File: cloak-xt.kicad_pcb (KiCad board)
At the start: 2 copper layers, 289.7 x 98 mm, 187 parts, among them J1 JST, Q1 Q_PMOS_GSD, Q2 Q_PMOS_GSD, U1 STM32F072CBT6, U3 XC6206PxxxMR-Regulator_Linear

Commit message: Fixed and ignore silkscreen clipping
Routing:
- net COL2: track 324.5 -> 321.8 mm
- net ROW2: track 375.8 -> 373.7 mm
- net COL1: track 329.9 -> 328.1 mm
- net COL0: track 384.0 -> 382.2 mm
- net Net-(D29-A): track 29.4 -> 28.4 mm
- net COL4: track 271.9 -> 271.0 mm
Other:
- board text added: "switch center"

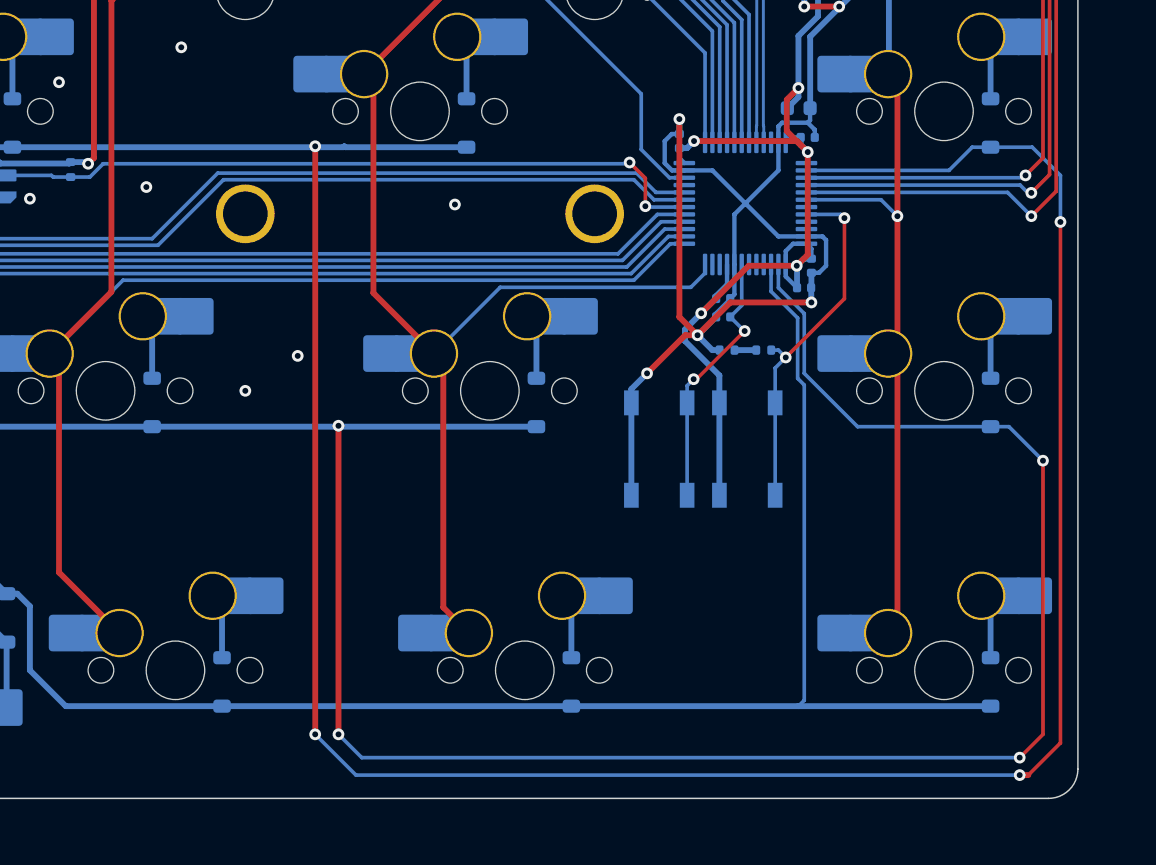
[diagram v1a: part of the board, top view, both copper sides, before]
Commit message: Fix PF/PC pins and change LED pin to B8
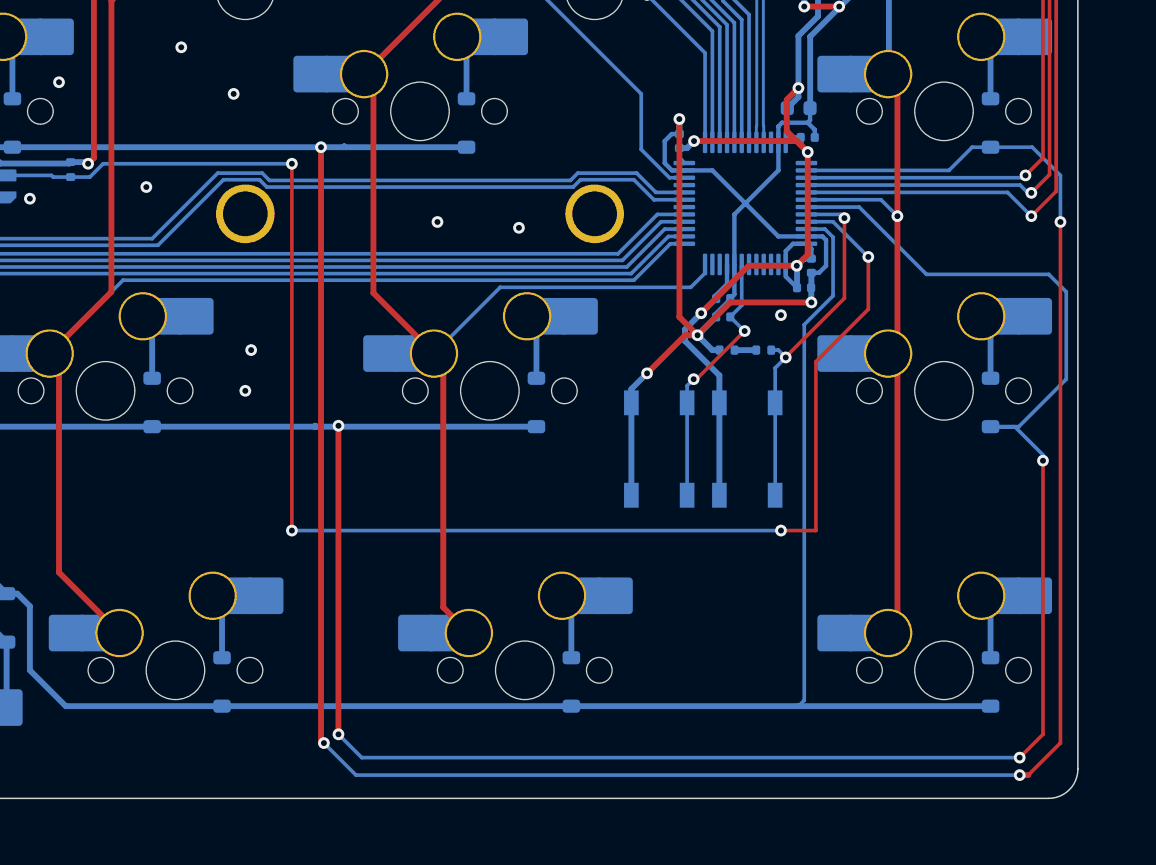
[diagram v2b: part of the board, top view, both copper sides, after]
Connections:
- U1 pad 18: LED -> /B0
- U1 pad 2: ROW3 -> /C13
- U1 pad 3: ROW4 -> /C14
- U1 pad 43: /B7 -> ROW3
- U1 pad 45: /B8 -> LED
- U1 pad 46: /B9 -> ROW4
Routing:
- net LED: track 49.1 -> 105.9 mm, vias 2 -> 4
- net ROW3: track 356.0 -> 366.4 mm
- net ROW4: track 318.9 -> 322.6 mm
- net GND: vias 51 -> 54

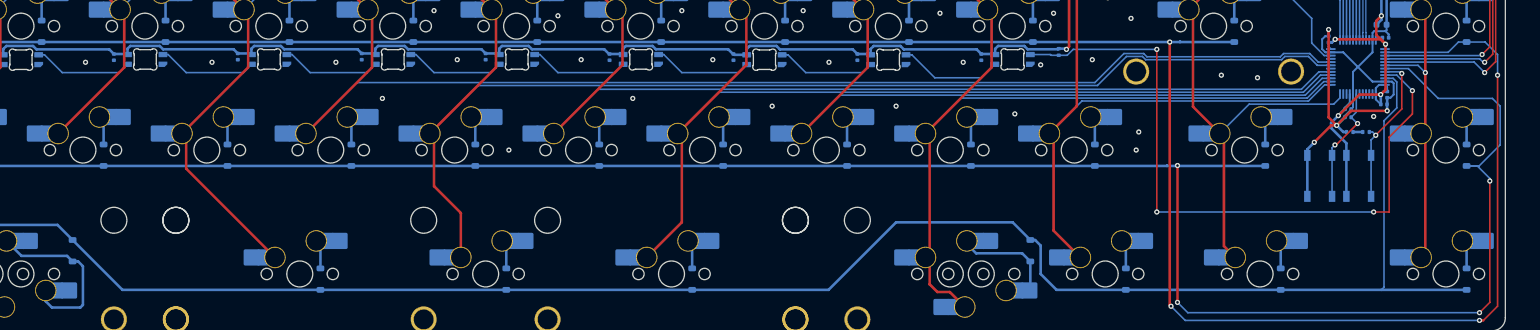
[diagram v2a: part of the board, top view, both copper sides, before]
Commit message: Fix GND and add vias
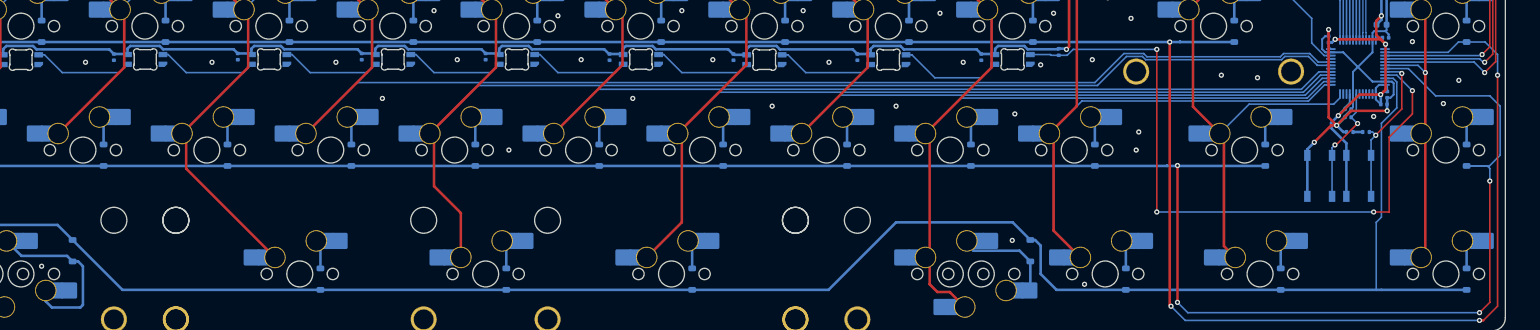
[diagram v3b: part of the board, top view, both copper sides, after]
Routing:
- net ROW3: track 366.4 -> 368.2 mm
- net GND: vias 54 -> 60
